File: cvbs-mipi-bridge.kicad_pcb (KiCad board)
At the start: 4 copper layers, 55 x 70 mm, 114 parts, among them IC1 ADV7282-M, IC2 TLV70018, IC4 SN74AUP1G17DCKR, IC5 SN74AUP1G17DCKR, J1 WE_68715014522, J2 1053131102, J3 KLPX-0848A-2-Y, J4 KLPX-0848A-2-Y, J5 KLPX-0848A-2-Y, J6 KLPX-0848A-2-Y, J7 61300211121, Q1 BSS138APW, Q2 BSS138APW, Q3 BSS138APW, Q4 BSS138APW, Y1 ABM8G-28.63636MHZ-18-D2Y-T

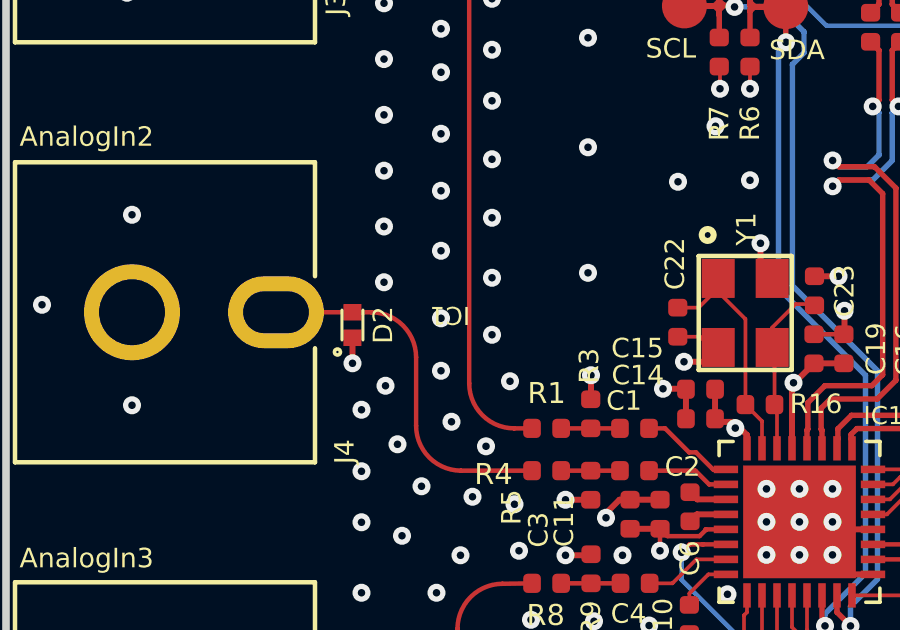
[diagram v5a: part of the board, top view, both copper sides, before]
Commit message: PCB: Clean up doubled IC1 reference designator on F.Silkscreen
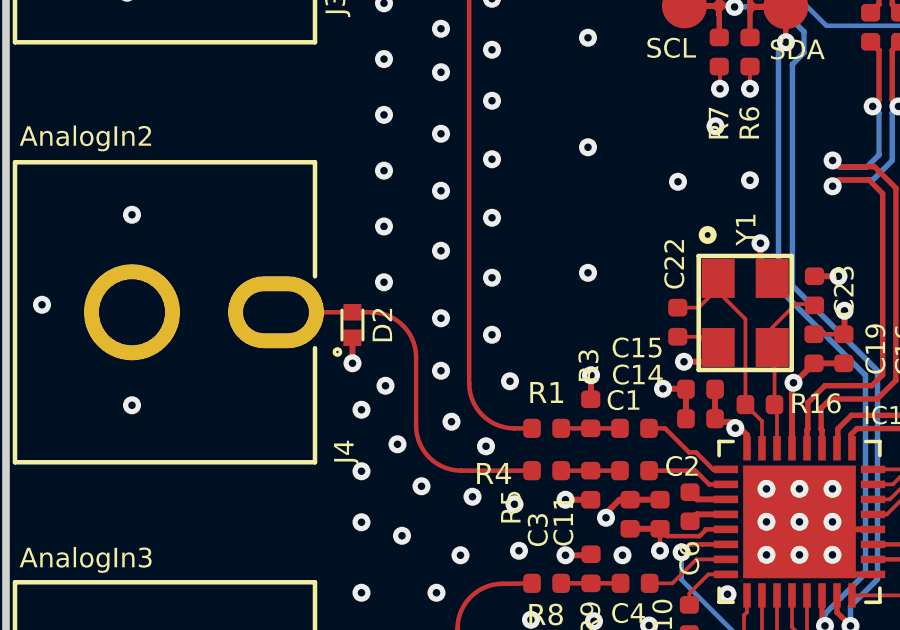
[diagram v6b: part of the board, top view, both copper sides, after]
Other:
- board text removed: "IC1"
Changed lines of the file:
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@@
   (gr_line (start 111.7 56) (end 166.7 56) (layer "Edge.Cuts") (width 0.254))
   (gr_line (start 111.7 126) (end 166.7 126) (layer "Edge.Cuts") (width 0.254))
-  (gr_text "IC1" (at 126.5 84.1 -180) (layer "F.SilkS")
-    (effects (font (size 0.6 0.6) (thickness 0.15)))
-  )
   (gr_text "AGPO2" (at 159.3 79.85 90) (layer "F.SilkS")
     (effects (font (size 0.65 0.65) (thickness 0.15)) (justify left))

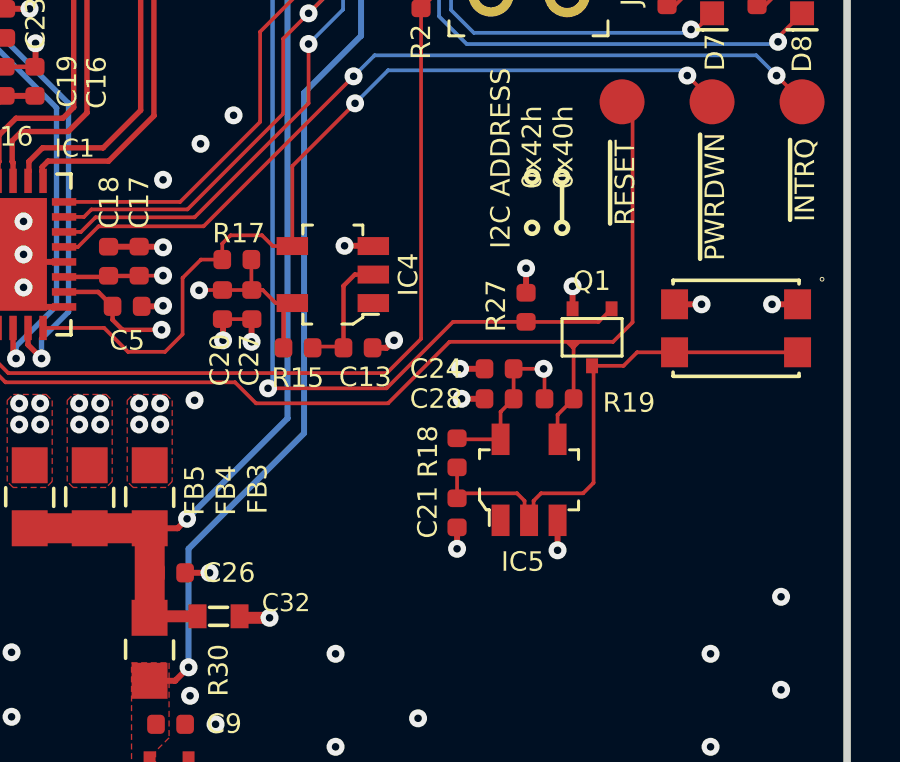
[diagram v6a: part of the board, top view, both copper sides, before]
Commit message: Update SN74AUP1G17DCKR symbol on SCH from local library
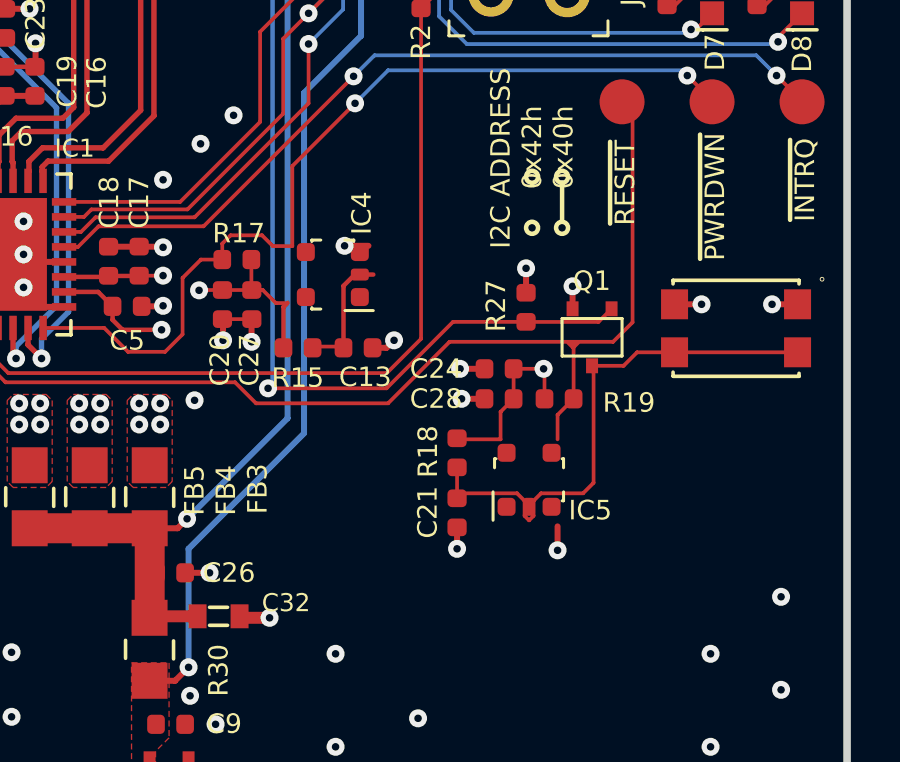
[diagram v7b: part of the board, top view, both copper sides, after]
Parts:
- IC4, IC5: footprint cvbs-mipi-bridge-footprints:SOT-753 -> antmicro-footprints:SOT-353
